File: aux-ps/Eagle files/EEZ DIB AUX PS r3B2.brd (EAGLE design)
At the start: 230.5 x 60 mm, 82 parts, among them IC1 BD00FC0WFP-E2, IC2 MAX31760AEE+, J1 PF0030/PC, J2 4907, J3 4907, J4 SWEB 8094 AU/GN, Q1 BTA26-600, Q2 BTA26-600, Q3 2N7002, Q4 2N7002, Q5 2N7002, SW1 DF62J12S2AHQA, SW2 OS102011MA1QN1C, X1 39-28-1063, X2 39-30-1039, X3 DS1013-16SSIB1, X4 47053-1000, X5 N.C.

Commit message: AUX-PS softstart pull-downs changed
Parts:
- R1, R3: value 2K2 -> 1K
- R10, R5: value 47K -> 4K7
- R23: value 47K -> 39K
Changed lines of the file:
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@@
 <grid distance="2.5" unitdist="mil" unit="mil" style="lines" multiple="40" display="no" altdistance="12.5" altunitdist="mil" altunit="mil"/>
 <layers>
-<layer number="1" name="Top" color="11" fill="1" visible="yes" active="yes"/>
+<layer number="1" name="Top" color="11" fill="1" visible="no" active="yes"/>
 <layer number="2" name="Route2" color="1" fill="3" visible="no" active="no"/>
 <layer number="3" name="Route3" color="4" fill="3" visible="no" active="no"/>
@@
 <layer number="14" name="Route14" color="1" fill="6" visible="no" active="no"/>
 <layer number="15" name="Route15" color="4" fill="6" visible="no" active="no"/>
-<layer number="16" name="Bottom" color="1" fill="1" visible="yes" active="yes"/>
-<layer number="17" name="Pads" color="6" fill="1" visible="yes" active="yes"/>
-<layer number="18" name="Vias" color="6" fill="1" visible="yes" active="yes"/>
-<layer number="19" name="Unrouted" color="6" fill="1" visible="yes" active="yes"/>
+<layer number="16" name="Bottom" color="1" fill="1" visible="no" active="yes"/>
+<layer number="17" name="Pads" color="6" fill="1" visible="no" active="yes"/>
+<layer number="18" name="Vias" color="6" fill="1" visible="no" active="yes"/>
+<layer number="19" name="Unrouted" color="6" fill="1" visible="no" active="yes"/>
 <layer number="20" name="Dimension" color="12" fill="1" visible="yes" active="yes"/>
 <layer number="21" name="tPlace" color="7" fill="1" visible="yes" active="yes"/>
 <layer number="22" name="bPlace" color="13" fill="1" visible="no" active="yes"/>
-<layer number="23" name="tOrigins" color="15" fill="1" visible="yes" active="yes"/>
+<layer number="23" name="tOrigins" color="15" fill="1" visible="no" active="yes"/>
 <layer number="24" name="bOrigins" color="15" fill="1" visible="no" active="yes"/>
 <layer number="25" name="tNames" color="7" fill="1" visible="yes" active="yes"/>
 <layer number="26" name="bNames" color="13" fill="1" visible="no" active="yes"/>
-<layer number="27" name="tValues" color="14" fill="1" visible="no" active="yes"/>
+<layer number="27" name="tValues" color="14" fill="1" visible="yes" active="yes"/>
 <layer number="28" name="bValues" color="11" fill="1" visible="no" active="yes"/>
 <layer number="29" name="tStop" color="15" fill="1" visible="yes" active="yes"/>
@@
 <layer number="41" name="tRestrict" color="4" fill="10" visible="no" active="yes"/>
 <layer number="42" name="bRestrict" color="1" fill="10" visible="no" active="yes"/>
-<layer number="43" name="vRestrict" color="2" fill="10" visible="yes" active="yes"/>
+<layer number="43" name="vRestrict" color="2" fill="10" visible="no" active="yes"/>
 <layer number="44" name="Drills" color="7" fill="1" visible="no" active="yes"/>
 <layer number="45" name="Holes" color="7" fill="1" visible="no" active="yes"/>
@@
 <attribute name="VALUE" x="184.277" y="49.022" size="1.016" layer="27" ratio="10"/>
 </element>
-<element name="R3" library="rcl" package="R0805" value="2K2" x="167.0685" y="36.6395" smashed="yes" rot="R90">
+<element name="R3" library="rcl" package="R0805" value="1K" x="167.0685" y="36.6395" smashed="yes" rot="R90">
 <attribute name="NAME" x="168.275" y="36.068" size="1.016" layer="25" ratio="10"/>
-<attribute name="VALUE" x="167.4495" y="35.3695" size="1.016" layer="27" ratio="10" rot="R90"/>
-</element>
-<element name="R1" library="rcl" package="R0805" value="2K2" x="179.451" y="19.2405" smashed="yes" rot="R180">
+<attribute name="VALUE" x="167.5765" y="35.7505" size="1.016" layer="27" ratio="10" rot="R90"/>
+</element>
+<element name="R1" library="rcl" package="R0805" value="1K" x="179.451" y="19.2405" smashed="yes" rot="R180">
 <attribute name="NAME" x="178.6255" y="20.5105" size="1.016" layer="25" ratio="10"/>
 <attribute name="VALUE" x="180.6575" y="19.7485" size="1.016" layer="27" ratio="10" rot="R180"/>
@@
 <attribute name="VALUE" x="43.6626" y="14.5415" size="0.8128" layer="27" ratio="10" rot="SR0"/>
 </element>
-<element name="R23" library="rcl" package="R0805" value="47K" x="46.99" y="18.7325" smashed="yes" rot="R270">
+<element name="R23" library="rcl" package="R0805" value="39K" x="46.99" y="18.7325" smashed="yes" rot="R270">
 <attribute name="NAME" x="49.149" y="17.526" size="1.016" layer="25" ratio="10" rot="R90"/>
 <attribute name="VALUE" x="46.355" y="20.193" size="1.016" layer="27" ratio="10" rot="R270"/>
@@
 <attribute name="NAME" x="45.466" y="30.734" size="1.016" layer="25" ratio="10"/>
 </element>
-<element name="R5" library="rcl" package="R0805" value="47K" x="66.1035" y="39.1795" smashed="yes" rot="R180">
+<element name="R5" library="rcl" package="R0805" value="4K7" x="66.1035" y="39.1795" smashed="yes" rot="R180">
 <attribute name="NAME" x="65.278" y="40.3225" size="1.016" layer="25" ratio="10"/>
 <attribute name="VALUE" x="67.31" y="39.6875" size="1.016" layer="27" ratio="10" rot="R180"/>
 </element>
-<element name="R10" library="rcl" package="R0805" value="47K" x="62.1665" y="39.1795" smashed="yes" rot="R180">
+<element name="R10" library="rcl" package="R0805" value="4K7" x="62.1665" y="39.1795" smashed="yes" rot="R180">
 <attribute name="NAME" x="60.8965" y="40.3225" size="1.016" layer="25" ratio="10"/>
 <attribute name="VALUE" x="63.5" y="39.751" size="1.016" layer="27" ratio="10" rot="R180"/>

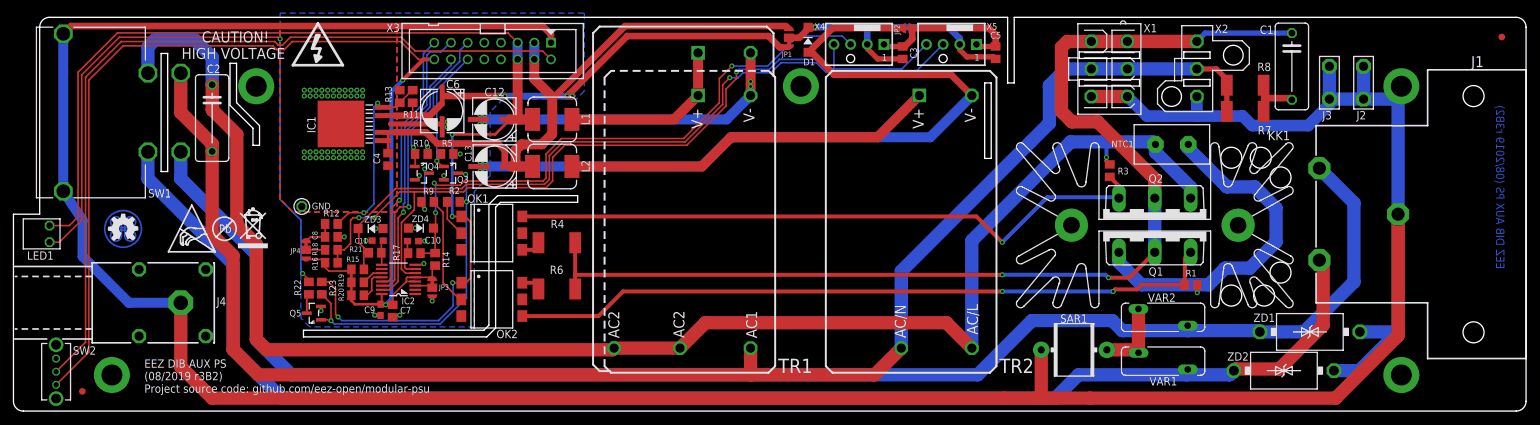
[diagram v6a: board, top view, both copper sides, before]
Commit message: AUX-PS SW2 replaced with tactile switch
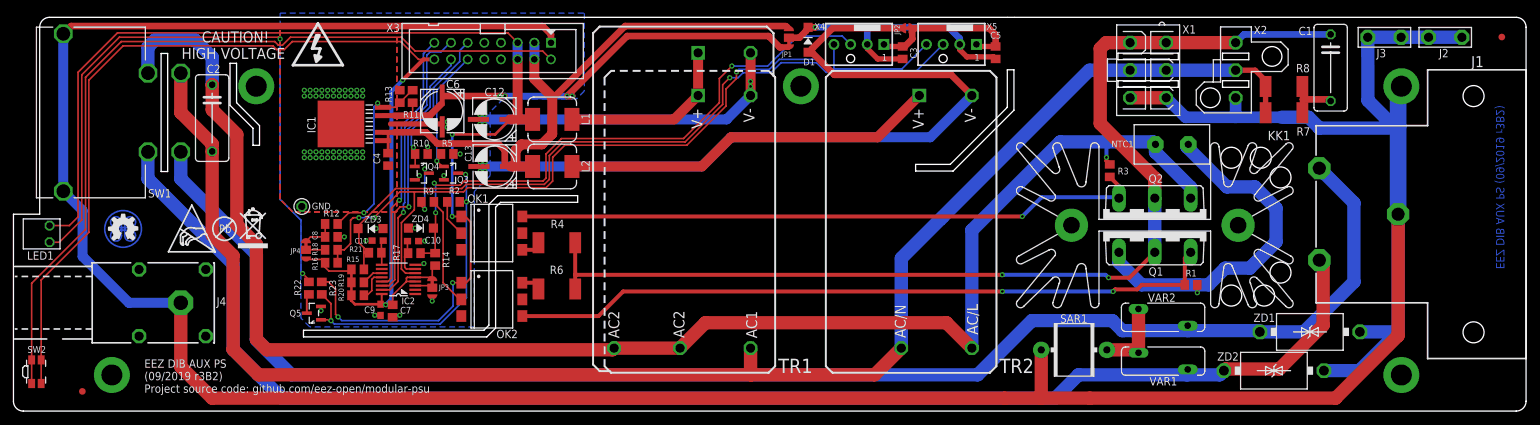
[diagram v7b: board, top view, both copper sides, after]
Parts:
- J2, J3: value 4907 -> 1-726388-2; device EEZ_connectors:PCB_TAB-4907 -> EEZ_connectors:PCB_TAB-4.8MM
- SW2: value OS102011MA1QN1C -> EVQP7A01P; device EEZ_switches:OS102011 -> EEZ_switches:PANASONIC_EVQP
- moved J2 14.2 mm to (218.2, 57.0), turned to 180 degrees
- moved J3 10.9 mm to (208.9, 57.0), turned to 0 degrees
- moved R7 5.91 mm to (193.6, 45.5)
- moved R8 5.91 mm to (193.6, 49.5)
- moved X1 5.91 mm to (172.9, 51.9)
- moved C1 5.91 mm to (200.7, 52.3)
- moved X2 5.91 mm to (186.2, 51.9)
- moved SW2 3.00 mm to (3.50, 6.00), turned to 90 degrees
- moved ZD2 1.52 mm to (192.1, 6.16)
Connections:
- net +3V3: now also SW2.2.1, SW2.2.2; no longer SW2.3
- net MBOOT: now also SW2.1.1, SW2.1.2; no longer SW2.2
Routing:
- net PE: track 477.4 -> 490.2 mm
- net AC_OUT_L: track 172.6 -> 167.7 mm
- net AC_N_OUT: track 237.6 -> 241.2 mm
- net MBOOT: track 122.0 -> 125.4 mm
- net N$71: track 99.3 -> 96.1 mm
- net AC_L_OUT: track 239.0 -> 239.9 mm
- net +3V3: track 181.9 -> 182.6 mm
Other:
- outline, holes or cut-outs redrawn
- board text added: "EEZ DIB AUX PS (09/2019 r3B2)"
- board text added: "EEZ DIB AUX PS (09/2019 r3B2) Project source code: github.com/eez-open/modular-psu"
- board text removed: "EEZ DIB AUX PS (08/2019 r3B2)"
- board text removed: "EEZ DIB AUX PS (08/2019 r3B2) Project source code: github.com/eez-open/modular-psu"

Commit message: AUX PS PCB improvements, DCM220 ZD2, ZD4 correction
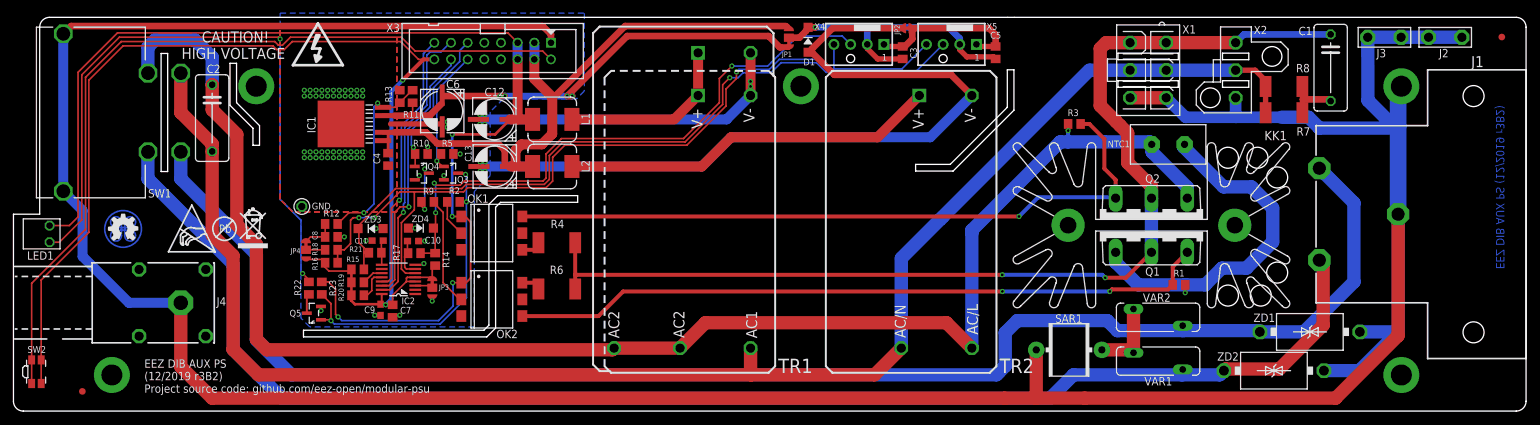
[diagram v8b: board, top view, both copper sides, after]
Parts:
- moved R3 8.93 mm to (161.7, 43.8), turned to 180 degrees
- moved R1 1.84 mm to (177.6, 19.2)
- moved SAR1 0.76 mm to (165.9, 9.33)
- moved VAR2 0.76 mm to (174.4, 14.3)
- moved VAR1 0.76 mm to (174.4, 7.61)
- moved NTC1 0.57 mm to (176.0, 40.6)
- moved KK1 0.51 mm to (173.4, 29.2)
- moved Q1 0.51 mm to (173.4, 27.4)
- moved Q2 0.51 mm to (173.4, 29.3)
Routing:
- net N$71: track 96.1 -> 106.0 mm
- net AC_N_IN: track 230.4 -> 233.4 mm
- net N$72: track 108.3 -> 107.0 mm
- net AC_L_OUT: track 239.9 -> 238.7 mm
- net AC_OUT_L: track 167.7 -> 166.9 mm
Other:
- board text added: "EEZ DIB AUX PS (12/2019 r3B2)"
- board text added: "EEZ DIB AUX PS (12/2019 r3B2) Project source code: github.com/eez-open/modular-psu"
- board text removed: "EEZ DIB AUX PS (09/2019 r3B2)"
- board text removed: "EEZ DIB AUX PS (09/2019 r3B2) Project source code: github.com/eez-open/modular-psu"
